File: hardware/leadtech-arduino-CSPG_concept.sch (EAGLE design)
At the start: 18 parts, among them IC1 CD4050B, J1 CON_HEADER_1X08-PTH, J2 CON_HEADER_1X08-PTH, J3 CON_HEADER_1X08-PTH, J4 CON_HEADER_1X06-PTH, J5 CON_HEADER_1X05-PTH, J6 CON_HEADER_1X02-PTH, J7 CON_HEADER_1X05-PTH, J8 CON_HEADER_1X08-PTH, P1 CON_HEADER_2X09, P2 CON_HEADER_2X09, SW1 SW_TACT_2P-3X6

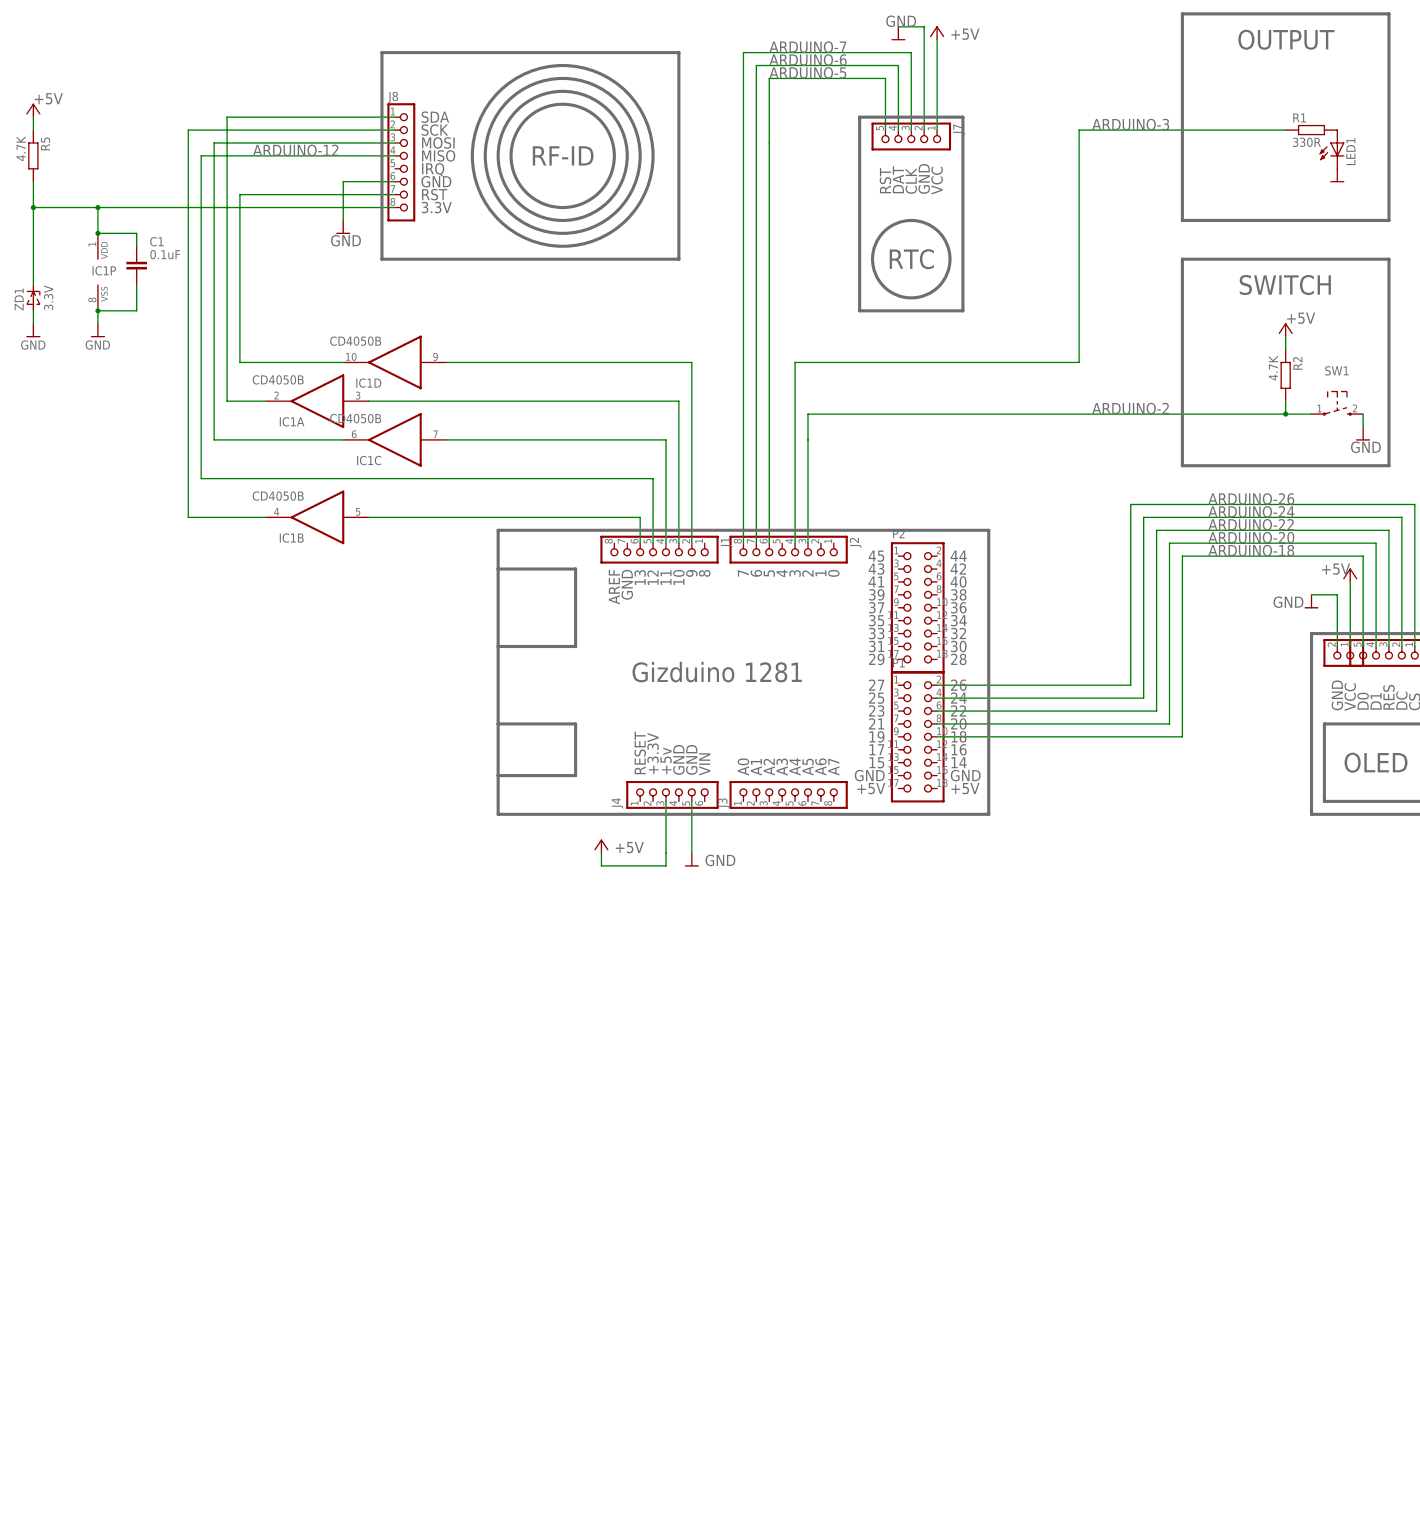
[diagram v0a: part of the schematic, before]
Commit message: add atmega1281 mcu
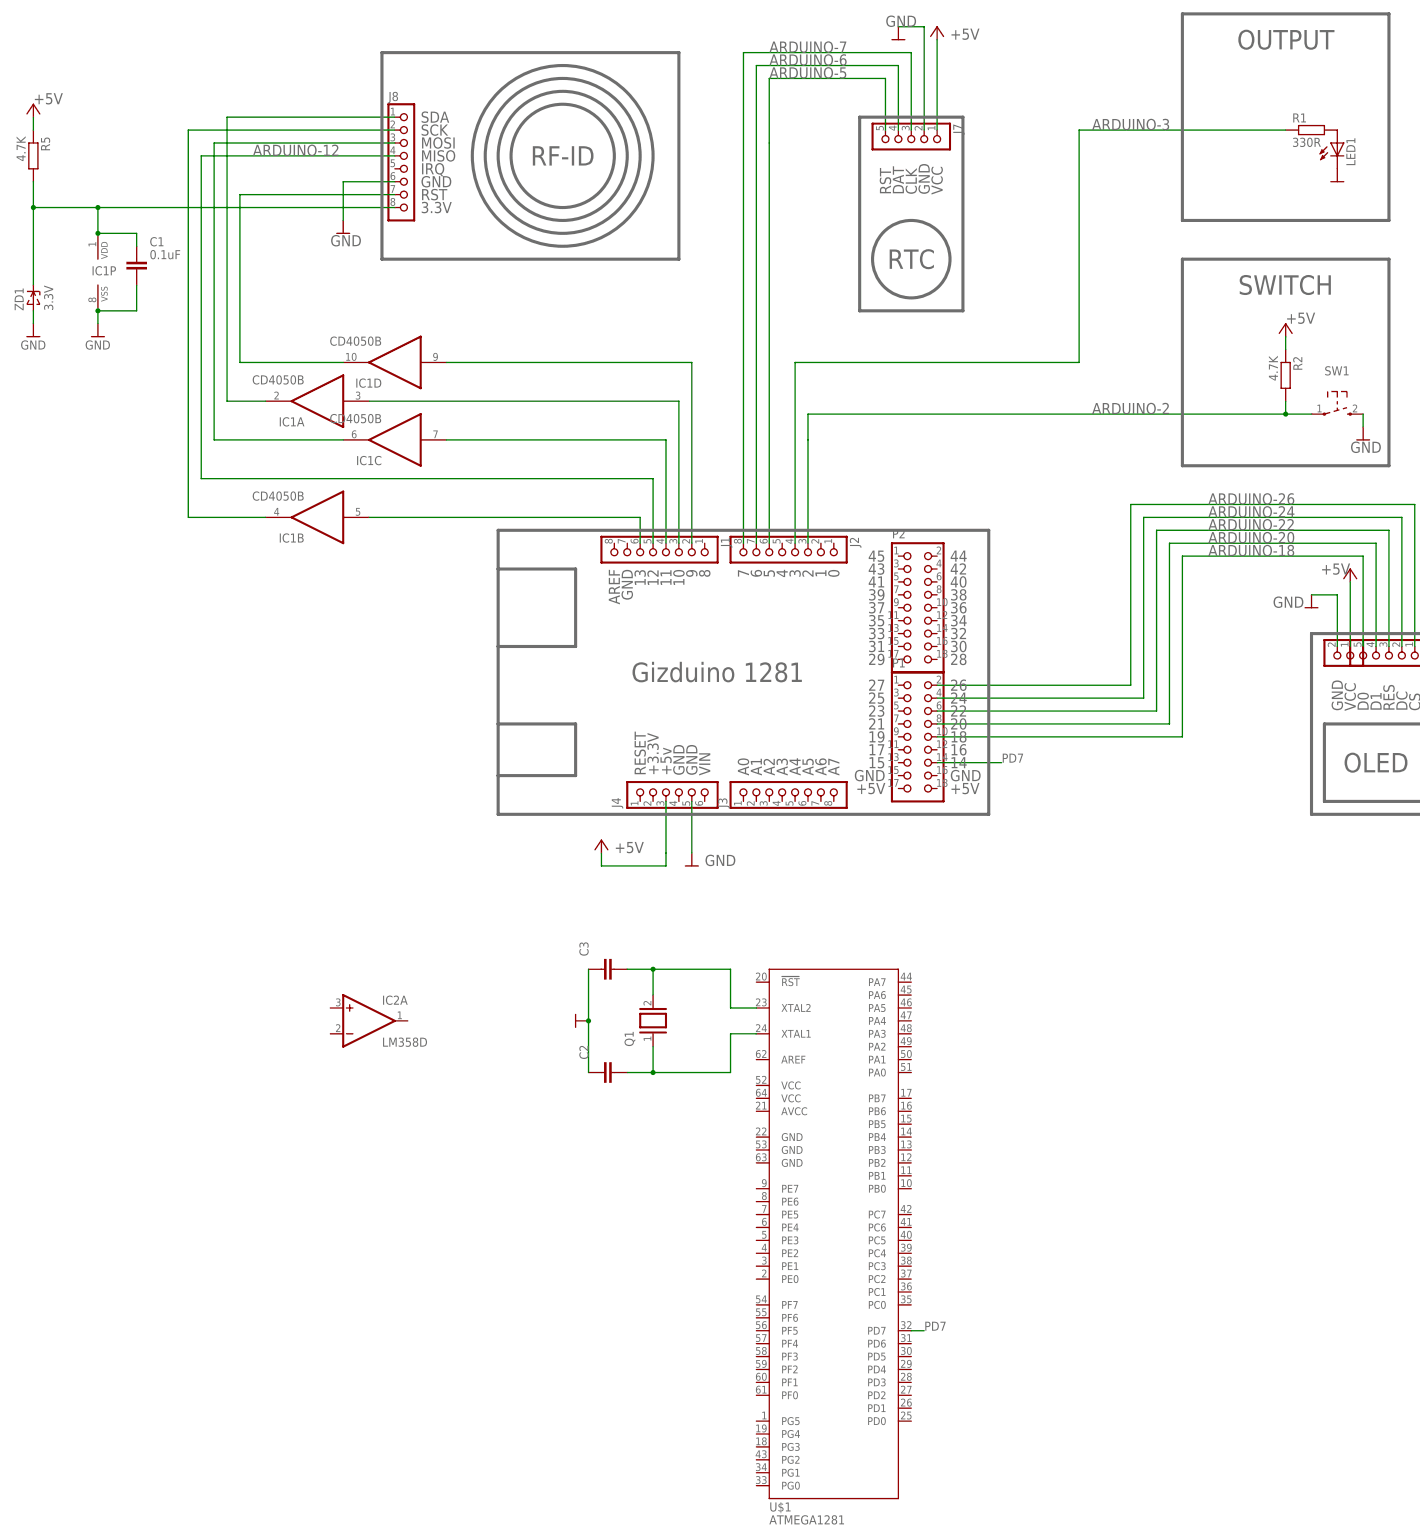
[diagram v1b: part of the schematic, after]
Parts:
- added C2, C3: (no value), dp_devices.v6:CAPACITOR_NPOL-0805
- added IC2: LM358D, linear:LM358D
- added Q1: (no value), special:XTAL/S
- added U$1: ATMEGA1281, trosh_devices.eagle.v9:ATMEGA1281
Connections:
- new net N$10: C2.2, Q1.1, U$1.XTAL1
- new net N$8: C3.2, Q1.2, U$1.XTAL2
- new net PD7: P1.14, U$1.PD7
- net GND: now also C2.1, C3.1
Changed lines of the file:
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@@
 <?xml version="1.0" encoding="utf-8"?>
 <!DOCTYPE eagle SYSTEM "eagle.dtd">
-<eagle version="9.1.3">
+<eagle version="9.4.2">
 <drawing>
 <settings>
@@
 <part name="GND8" library="dp_devices.v6" deviceset="SUPPLY_GND" device=""/>
 <part name="C1" library="dp_devices.v6" deviceset="CAPACITOR_NPOL" device="-PTH_0.1&quot;" value="0.1uF"/>
+<part name="U$1" library="trosh_devices.eagle.v9" deviceset="ATMEGA1281" device=""/>
+<part name="IC2" library="linear" library_urn="urn:adsk.eagle:library:262" deviceset="LM358" device="D" package3d_urn="urn:adsk.eagle:package:16404/2"/>
+<part name="Q1" library="special" library_urn="urn:adsk.eagle:library:367" deviceset="XTAL/S" device="" package3d_urn="urn:adsk.eagle:package:26647/2"/>
+<part name="C2" library="dp_devices.v6" deviceset="CAPACITOR_NPOL" device="-0805"/>
+<part name="C3" library="dp_devices.v6" deviceset="CAPACITOR_NPOL" device="-0805"/>
+<part name="GND9" library="dp_devices.v6" deviceset="SUPPLY_GND" device=""/>
 </parts>
 <sheets>
@@
 <wire x1="116.84" y1="40.64" x2="101.6" y2="40.64" width="0.6096" layer="95"/>
 <wire x1="101.6" y1="25.4" x2="116.84" y2="25.4" width="0.6096" layer="95"/>
-<wire x1="116.84" y1="25.4" x2="116.84" y2="17.78" width="0.6096" layer="95"/>
-<wire x1="116.84" y1="17.78" x2="116.84" y2="15.24" width="0.6096" layer="95"/>
+<wire x1="116.84" y1="25.4" x2="116.84" y2="15.24" width="0.6096" layer="95"/>
 <wire x1="116.84" y1="15.24" x2="101.6" y2="15.24" width="0.6096" layer="95"/>
 <text x="144.78" y="35.56" size="3.81" layer="95" align="center">Gizduino 1281</text>
@@
 <instance part="J5" gate="J" x="276.86" y="40.64" smashed="yes" rot="R270"/>
 <instance part="J6" gate="J" x="269.24" y="40.64" smashed="yes" rot="R270"/>
-<instance part="J7" gate="J" x="182.88" y="142.24" rot="R270"/>
-<instance part="J8" gate="J" x="81.28" y="137.16"/>
-<instance part="LED1" gate="LED" x="266.7" y="139.7"/>
-<instance part="R1" gate="R" x="261.62" y="142.24"/>
+<instance part="J7" gate="J" x="182.88" y="142.24" smashed="yes" rot="R270">
+<attribute name="NAME" x="191.135" y="143.51" size="1.778" layer="95" rot="R270"/>
+</instance>
+<instance part="J8" gate="J" x="81.28" y="137.16" smashed="yes">
+<attribute name="NAME" x="80.01" y="147.955" size="1.778" layer="95"/>
+</instance>
+<instance part="LED1" gate="LED" x="266.7" y="139.7" smashed="yes">
+<attribute name="NAME" x="270.256" y="135.128" size="1.778" layer="95" rot="R90"/>
+<attribute name="VALUE" x="272.415" y="135.128" size="1.778" layer="96" rot="R90"/>
+</instance>
+<instance part="R1" gate="R" x="261.62" y="142.24" smashed="yes">
+<attribute name="NAME" x="257.81" y="143.7386" size="1.778" layer="95" font="vector"/>
+<attribute name="VALUE" x="257.81" y="138.938" size="1.778" layer="96" font="vector"/>
+</instance>
 <instance part="SW1" gate="SW" x="266.7" y="86.36" smashed="yes">
 <attribute name="NAME" x="264.16" y="93.98" size="1.778" layer="95" font="vector"/>
@@
 <instance part="GND5" gate="G$1" x="266.7" y="132.08" smashed="yes"/>
 <instance part="+5V4" gate="SUPPLY" x="256.54" y="101.6" smashed="yes"/>
-<instance part="R2" gate="R" x="256.54" y="93.98" rot="R270"/>
+<instance part="R2" gate="R" x="256.54" y="93.98" smashed="yes" rot="R270">
+<attribute name="NAME" x="258.0386" y="97.79" size="1.778" layer="95" font="vector" rot="R270"/>
+<attribute name="VALUE" x="253.238" y="97.79" size="1.778" layer="96" font="vector" rot="R270"/>
+</instance>
 <instance part="GND6" gate="G$1" x="71.12" y="121.92" smashed="yes"/>
-<instance part="ZD1" gate="G$1" x="10.16" y="109.22" rot="R90"/>
+<instance part="ZD1" gate="G$1" x="10.16" y="109.22" smashed="yes" rot="R90">
+<attribute name="NAME" x="8.255" y="106.68" size="1.778" layer="95" font="vector" rot="R90"/>
+<attribute name="VALUE" x="14.0589" y="106.68" size="1.778" layer="96" font="vector" rot="R90"/>
+</instance>
 <instance part="+5V5" gate="SUPPLY" x="10.16" y="144.78" smashed="yes"/>
 <instance part="GND7" gate="G$1" x="10.16" y="101.6" smashed="yes"/>
-<instance part="R5" gate="R" x="10.16" y="137.16" rot="R270"/>
-<instance part="IC1" gate="A" x="66.04" y="88.9" rot="R180"/>
-<instance part="IC1" gate="B" x="66.04" y="66.04" rot="R180"/>
-<instance part="IC1" gate="C" x="81.28" y="81.28" rot="R180"/>
-<instance part="IC1" gate="D" x="81.28" y="96.52" rot="R180"/>
-<instance part="IC1" gate="P" x="22.86" y="114.3"/>
+<instance part="R5" gate="R" x="10.16" y="137.16" smashed="yes" rot="R270">
+<attribute name="NAME" x="11.6586" y="140.97" size="1.778" layer="95" font="vector" rot="R270"/>
+<attribute name="VALUE" x="6.858" y="140.97" size="1.778" layer="96" font="vector" rot="R270"/>
+</instance>
+<instance part="IC1" gate="A" x="66.04" y="88.9" smashed="yes" rot="R180">
+<attribute name="NAME" x="63.5" y="85.725" size="1.778" layer="95" rot="R180"/>
+<attribute name="VALUE" x="63.5" y="93.98" size="1.778" layer="96" rot="R180"/>
+</instance>
+<instance part="IC1" gate="B" x="66.04" y="66.04" smashed="yes" rot="R180">
+<attribute name="NAME" x="63.5" y="62.865" size="1.778" layer="95" rot="R180"/>
+<attribute name="VALUE" x="63.5" y="71.12" size="1.778" layer="96" rot="R180"/>
+</instance>
+<instance part="IC1" gate="C" x="81.28" y="81.28" smashed="yes" rot="R180">
+<attribute name="NAME" x="78.74" y="78.105" size="1.778" layer="95" rot="R180"/>
+<attribute name="VALUE" x="78.74" y="86.36" size="1.778" layer="96" rot="R180"/>
+</instance>
+<instance part="IC1" gate="D" x="81.28" y="96.52" smashed="yes" rot="R180">
+<attribute name="NAME" x="78.74" y="93.345" size="1.778" layer="95" rot="R180"/>
+<attribute name="VALUE" x="78.74" y="101.6" size="1.778" layer="96" rot="R180"/>
+</instance>
+<instance part="IC1" gate="P" x="22.86" y="114.3" smashed="yes">
+<attribute name="NAME" x="21.59" y="113.665" size="1.778" layer="95"/>
+</instance>
 <instance part="GND8" gate="G$1" x="22.86" y="101.6" smashed="yes"/>
-<instance part="C1" gate="C" x="30.48" y="114.3"/>
+<instance part="C1" gate="C" x="30.48" y="114.3" smashed="yes">
+<attribute name="NAME" x="33.02" y="119.38" size="1.778" layer="95"/>
+<attribute name="VALUE" x="33.02" y="116.84" size="1.778" layer="96"/>
+</instance>
+<instance part="U$1" gate="U" x="167.64" y="-76.2" smashed="yes">
+<attribute name="NAME" x="154.94" y="-129.54" size="1.778" layer="95"/>
+<attribute name="VALUE" x="154.94" y="-132.08" size="1.778" layer="95"/>
+</instance>
+<instance part="IC2" gate="A" x="76.2" y="-33.02" smashed="yes">
+<attribute name="NAME" x="78.74" y="-29.845" size="1.778" layer="95"/>
+<attribute name="VALUE" x="78.74" y="-38.1" size="1.778" layer="96"/>
+</instance>
+<instance part="Q1" gate="G$1" x="132.08" y="-33.02" smashed="yes" rot="R90">
+<attribute name="NAME" x="128.27" y="-38.1" size="1.778" layer="95" rot="R90"/>
+<attribute name="VALUE" x="137.16" y="-38.1" size="1.778" layer="96" rot="R90"/>
+</instance>
+<instance part="C2" gate="C" x="124.46" y="-43.18" smashed="yes" rot="R90">
+<attribute name="NAME" x="119.38" y="-40.64" size="1.778" layer="95" rot="R90"/>
+<attribute name="VALUE" x="121.92" y="-40.64" size="1.778" layer="96" rot="R90"/>
+</instance>
+<instance part="C3" gate="C" x="124.46" y="-22.86" smashed="yes" rot="R90">
+<attribute name="NAME" x="119.38" y="-20.32" size="1.778" layer="95" rot="R90"/>
+<attribute name="VALUE" x="121.92" y="-20.32" size="1.778" layer="96" rot="R90"/>
+</instance>
+<instance part="GND9" gate="G$1" x="116.84" y="-33.02" smashed="yes" rot="R270"/>
 </instances>
 <busses>
@@
 <wire x1="30.48" y1="106.68" x2="30.48" y2="111.76" width="0.1524" layer="91"/>
 <junction x="22.86" y="106.68"/>
+</segment>
+<segment>
+<pinref part="C3" gate="C" pin="1"/>
+<pinref part="GND9" gate="G$1" pin="GND"/>
+<wire x1="119.38" y1="-22.86" x2="119.38" y2="-33.02" width="0.1524" layer="91"/>
+<pinref part="C2" gate="C" pin="1"/>
+<wire x1="119.38" y1="-33.02" x2="119.38" y2="-43.18" width="0.1524" layer="91"/>
+<junction x="119.38" y="-33.02"/>
 </segment>
 </net>
@@
 </segment>
 </net>
+<net name="N$8" class="0">
+<segment>
+<pinref part="U$1" gate="U" pin="XTAL2"/>
+<wire x1="152.4" y1="-30.48" x2="147.32" y2="-30.48" width="0.1524" layer="91"/>
+<wire x1="147.32" y1="-30.48" x2="147.32" y2="-22.86" width="0.1524" layer="91"/>
+<wire x1="147.32" y1="-22.86" x2="132.08" y2="-22.86" width="0.1524" layer="91"/>
+<pinref part="Q1" gate="G$1" pin="2"/>
+<wire x1="132.08" y1="-22.86" x2="132.08" y2="-27.94" width="0.1524" layer="91"/>
+<pinref part="C3" gate="C" pin="2"/>
+<wire x1="127" y1="-22.86" x2="132.08" y2="-22.86" width="0.1524" layer="91"/>
+<junction x="132.08" y="-22.86"/>
+</segment>
+</net>
+<net name="N$10" class="0">
+<segment>
+<pinref part="U$1" gate="U" pin="XTAL1"/>
+<wire x1="152.4" y1="-35.56" x2="147.32" y2="-35.56" width="0.1524" layer="91"/>
+<wire x1="147.32" y1="-35.56" x2="147.32" y2="-43.18" width="0.1524" layer="91"/>
+<wire x1="147.32" y1="-43.18" x2="132.08" y2="-43.18" width="0.1524" layer="91"/>
+<pinref part="Q1" gate="G$1" pin="1"/>
+<wire x1="132.08" y1="-43.18" x2="132.08" y2="-38.1" width="0.1524" layer="91"/>
+<pinref part="C2" gate="C" pin="2"/>
+<wire x1="127" y1="-43.18" x2="132.08" y2="-43.18" width="0.1524" layer="91"/>
+<junction x="132.08" y="-43.18"/>
+</segment>
+</net>
+<net name="PD7" class="0">
+<segment>
+<pinref part="U$1" gate="U" pin="PD7"/>
+<wire x1="182.88" y1="-93.98" x2="185.42" y2="-93.98" width="0.1524" layer="91"/>
+<label x="185.42" y="-93.98" size="1.778" layer="95"/>
+</segment>
+<segment>
+<pinref part="P1" gate="P" pin="14"/>
+<wire x1="187.96" y1="17.78" x2="200.66" y2="17.78" width="0.1524" layer="91"/>
+<label x="200.66" y="17.78" size="1.778" layer="95"/>
+</segment>
+</net>

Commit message: started routing schematic
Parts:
- added C4, C6, C7: 0.1uF, rcl:C-EUC0603
- added C5: 10uF, rcl:C-EUC0805
- added L1, L2: 800mA, dp_devices.v6:FERRITE-0805
- added R3, R4: 27R, dp_devices.v6:RESISTOR-0603
- added R6: 1.5K, dp_devices.v6:RESISTOR-0603
- added U1: DS1302, trosh_devices.eagle.v9:DS1302
- added U2: MFRC522, trosh_devices.eagle.v9:MFRC522
- added U3: PL2303HX, trosh_devices.eagle.v9:PL2303HX
- added USB1: USB-F-MINI-B, dp_devices.v6:CON-USB-F-MINI-B
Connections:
- new net N$11: R3.1, USB1USB.D-
- new net N$12: R4.1, R6.1, USB1USB.D+
- new net N$13: R3.2, U3.DM
- new net N$14: R4.2, U3.DP
- new net N$15: L1.2, USB1USB.VUSB
- new net N$16: L2.2, USB1USB.GND
- new net N$17: C7.1, U3.VDD_325
- new net VO33: C4.1, R6.2, U3.VO_33
- new net VUSB: C5.1, C6.2, L1.1, U3.RESET_N, U3.VDD_5
- net GND: now also C4.2, C5.2, C6.1, C7.2, L2.1, U3.GND, U3.TEST

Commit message: building schematic
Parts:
- added C10, C11, C12, C13: 0.1uF, rcl:C-EUC0603
- added C8, C9: 100uF, dp_devices.v6:CAPACITOR_POL-CASE_B
- added D1: 1N4004, diode:1N4004
- added G1: CR2032H, battery:CR2032H
- added J9: CON_HEADER_1X02-PTH, dp_devices.v6:CON_HEADER_1X02-PTH
- added LED2: (no value), dp_devices.v6:LED-0805
- added R7, R8: 1K, dp_devices.v6:RESISTOR-0603
- added R9: 330R, dp_devices.v6:RESISTOR-0603
- added VREG1: 7805, dp_devices.v6:VREG_3PINS-TO-220V
- added XTAL1: 32.768khz, dp_devices.v6:OSC-XTALTC-26
- C2, C3: value (none) -> 22pF
- Q1: value (none) -> 16Mhz
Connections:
- new net N$18: R8.1, U3.RXD
- new net N$19: D1.A, J9.2
- new net N$20: C8.+, D1.C, VREG1.VIN
- new net N$21: LED2.C, R9.1
- new net N$22: U1.X2, XTAL1.2
- new net N$23: U1.X1, XTAL1.1
- new net N$24: G1.+, U1.VCC1
- new net RTC_CLOCK: U$1.PB7, U1.SCLK
- new net RTC_DATA: U$1.PB6, U1.I/O
- new net RTC_EN: U$1.PE3, U1.CE
- new net UART_RX: R7.2
- new net UART_TX: R8.2
- net +5V: now also C10.1, C11.1, C12.1, C13.1, C9.+, LED2.A, U$1.AVCC, U$1.VCC@1, U$1.VCC@2, U1.VCC2, VREG1.VOUT
- net GND: now also C10.2, C11.2, C12.2, C13.2, C2.2, C8.-, C9.-, G1.-, J9.1, R9.2, U$1.GND@1, U$1.GND@2, U$1.GND@3, U1.GND, VREG1.GND; no longer C2.1
- net N$10: now also C2.1; no longer C2.2
- net N$17: now also R7.1, U3.TXD; no longer C7.1, U3.VDD_325
- net VO33: now also C7.1, U3.RESET_N, U3.VDD_325
- net VUSB: no longer U3.RESET_N
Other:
- note added: "CALENDAR & CLOCK"
- note added: "POWER SUPPLY"
- note added: "TO DO: connect RX and TX"
- note added: "UC"
- note added: "USB INTERFACE"
- moved on the sheet: C1, C2, C3, C4, C5, C6, C7, IC1A, IC1B, IC1C, IC1D, IC1P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
